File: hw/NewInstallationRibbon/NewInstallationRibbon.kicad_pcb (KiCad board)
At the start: 2 copper layers, 99.7 x 84.5 mm, 34 parts, among them J1 +5V, J10 D4, J11 8 Pin, J12 LEFT, J13 RIGHT, J14 UP, J15 GND, J16 GND, J17 20 Pin, J18 DOWN, J19 R, J2 GND, J20 L, J21 START, J22 B_1, J23 B_2, J25 BRIGHT, J3 CLK, J4 SMS, J5 DW, J6 CL2, J7 D1, J8 D2, J9 D3

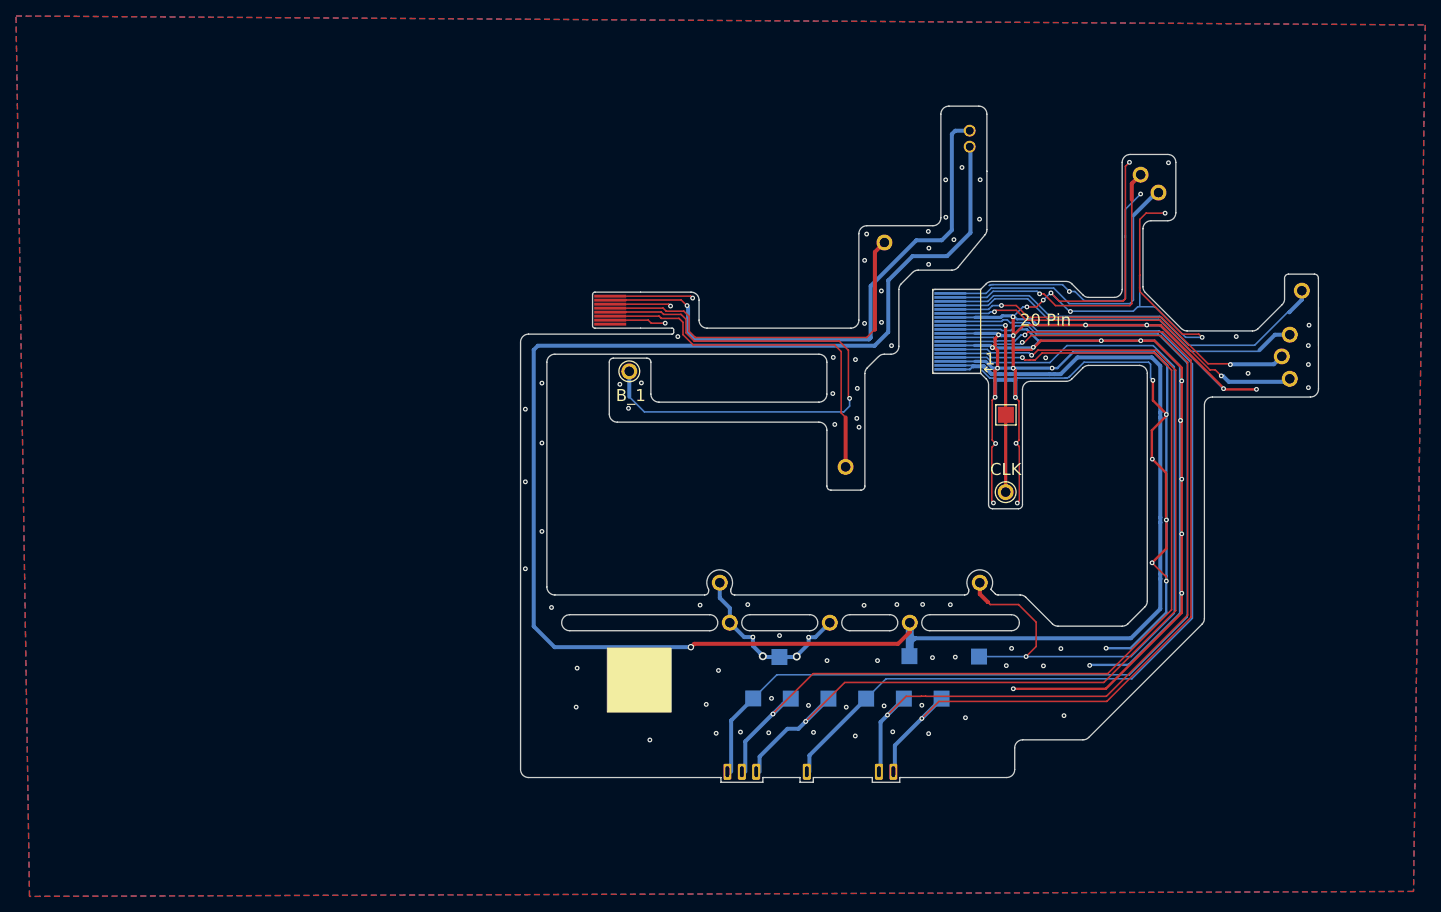
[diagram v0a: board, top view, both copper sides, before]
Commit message: Added LM358 op-amp for both audio channels.
Updated ribbon connector pin assignments, text labels, and tweaked board outline.
Gerbers updated for production.
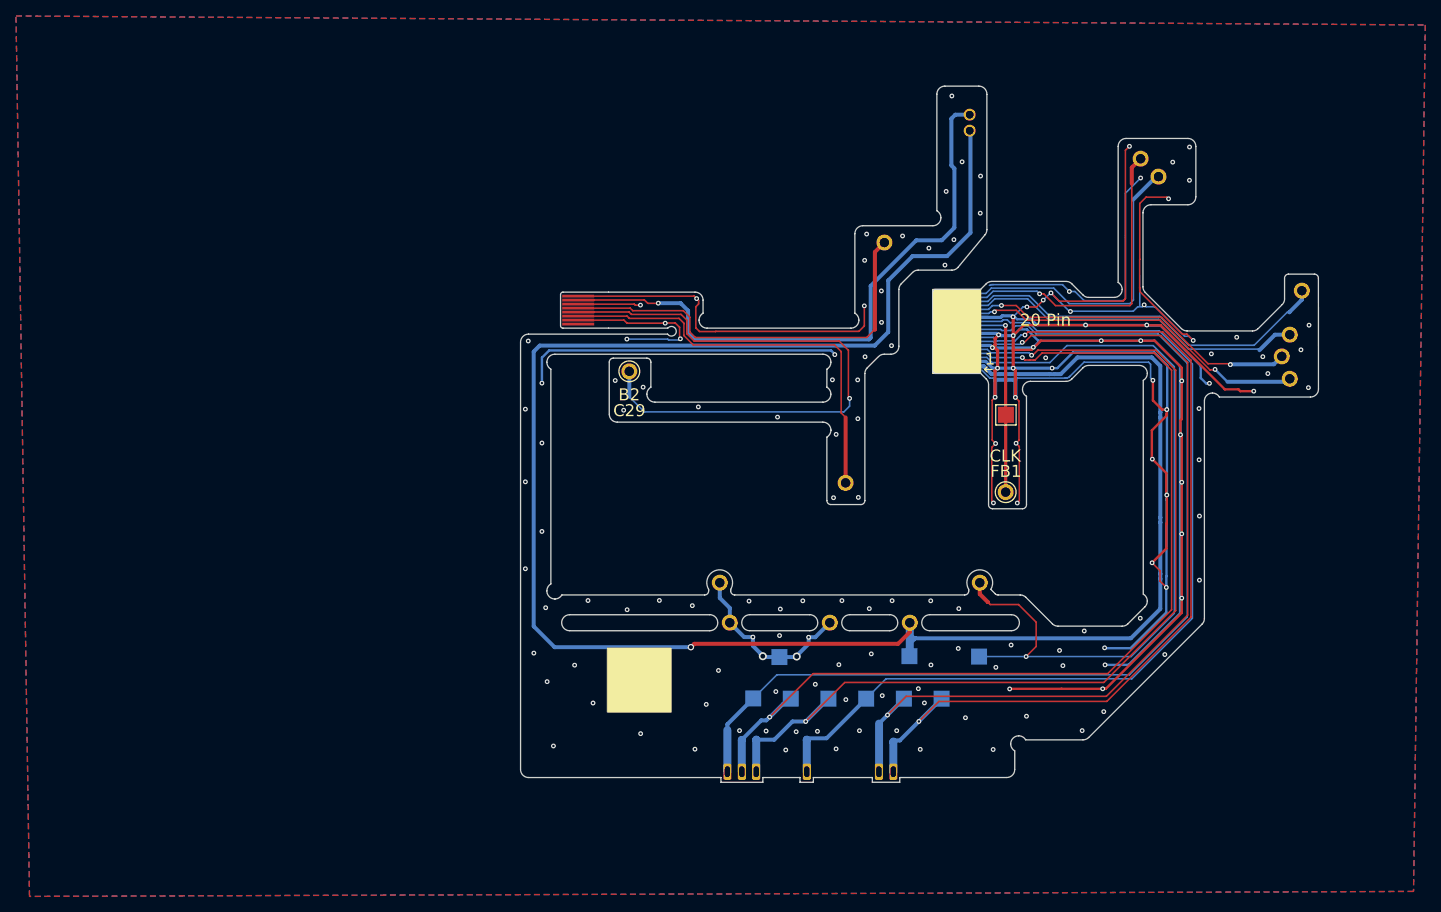
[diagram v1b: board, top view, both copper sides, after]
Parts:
- J1, J12, J13, J14, J15, J16, J18, J19, J2, J20, J21, J3, J4: footprint gg_lcd:TestPoint_THTPad_D2.5mm_Drill1.2mm_OneSided -> gg_lcd:TestPoint_THTPad_D2.5mm_Drill1.2mm
- J22: value B_1 -> B2; footprint gg_lcd:TestPoint_THTPad_D2.5mm_Drill1.2mm_OneSided -> gg_lcd:TestPoint_THTPad_D2.5mm_Drill1.2mm
- J23: value B_2 -> B1; footprint gg_lcd:TestPoint_THTPad_D2.5mm_Drill1.2mm_OneSided -> gg_lcd:TestPoint_THTPad_D2.5mm_Drill1.2mm
- moved J11 4.00 mm to (121.6, 84.5)
- moved J19 2.00 mm to (194.0, 65.6)
- moved J20 2.00 mm to (196.2, 67.8)
- moved J23 2.00 mm to (157.1, 106.1)
- moved J25 2.00 mm to (172.6, 60.1)
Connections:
- J11 pad 5: GG_BTN_1 -> GG_BTN_2
- J11 pad 6: GG_BTN_2 -> GG_BTN_1
- J22 pad 1: GG_BTN_1 -> GG_BTN_2
- J23 pad 1: GG_BTN_2 -> GG_BTN_1
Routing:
- net GND: track 577.2 -> 667.5 mm, vias 125 -> 158
- net GG_BTN_2: track 46.3 -> 77.6 mm, vias 0 -> 1
- net GG_BTN_1: track 73.6 -> 52.3 mm, vias 1 -> 0
- net GG_BRIGHT: track 72.5 -> 78.6 mm
- net GG_BTN_START: track 47.5 -> 51.5 mm
- net GG_AUDIO_R: track 40.4 -> 42.4 mm
- net GG_AUDIO_L: track 39.1 -> 41.1 mm
- net GG_+5V: track 262.6 -> 264.4 mm
- net GG_D2: track 125.6 -> 127.3 mm
- net GG_CL2: track 121.9 -> 123.2 mm
- net GG_D1: track 126.2 -> 127.3 mm
- net GG_D4: track 114.8 -> 115.7 mm
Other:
- board size 99.7 x 84.5 mm -> 99.7 x 87 mm

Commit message: Flex PCB updated:
- Use a single 24pin connection to the main board, pin out updated to match the main board.
- Various layout tweaks to improve installation by reducing some of the slack.
- Added rule areas around solder points to exclude copper fills to help align the solder points.
- Added guide holes for the top row of cartridge connector pins, and tweaked the other guide holes to help with install.
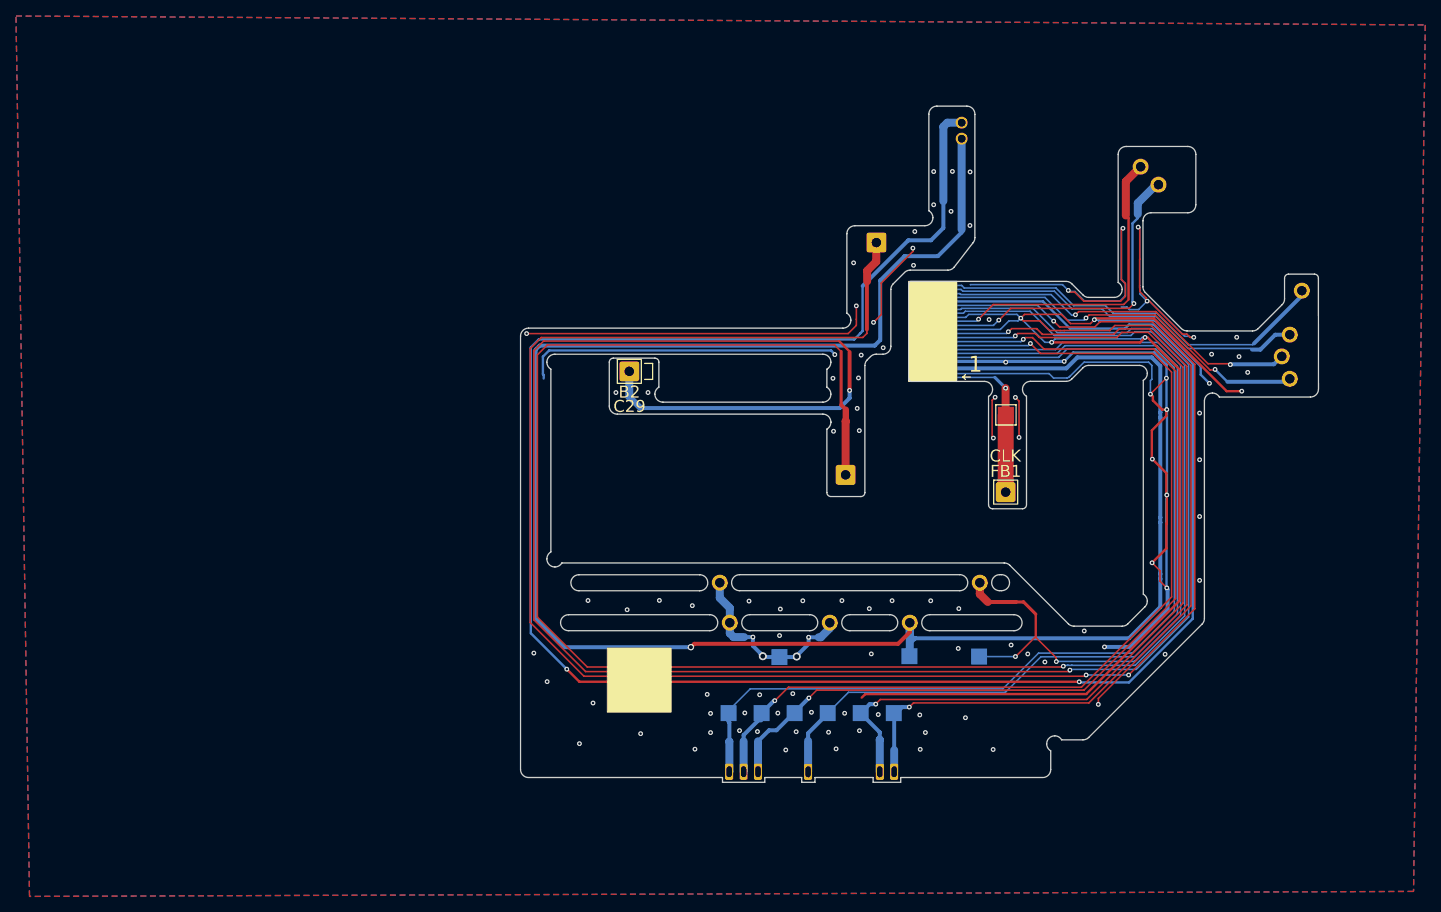
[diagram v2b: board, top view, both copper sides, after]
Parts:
- removed J11: 8 Pin, gg_lcd:Flex Connector 0.5mm 01x08Pin
- J17: value 20 Pin -> 24 Pin Flex Connector; footprint gg_lcd:Flex Connector 0.5mm 01x20Pin -> gg_lcd:Flex Connector 0.5mm 01x24Pin
- J21, J22, J23, J3: footprint gg_lcd:TestPoint_THTPad_D2.5mm_Drill1.2mm -> gg_lcd:TestPoint_THTPad_D2.5x2.5mm_Drill1.2mm
- moved TP7 6.24 mm to (163.2, 134.9)
- moved TP8 5.69 mm to (159.0, 134.9)
- moved TP6 5.14 mm to (154.9, 134.9)
- moved TP9 4.60 mm to (150.8, 134.9)
- moved TP10 4.07 mm to (146.6, 134.9)
- moved TP5 3.58 mm to (142.5, 134.9)
- moved J17 3.00 mm to (165.1, 87.2)
- moved J25 1.41 mm to (171.6, 61.1)
- moved J19 1.00 mm to (194.0, 66.6)
- moved J20 1.00 mm to (196.2, 68.8)
- moved J21 1.00 mm to (161.0, 76.0)
- moved J23 1.00 mm to (157.1, 105.1)
- moved J5 0.23 mm to (142.6, 142.2)
- moved J7 0.22 mm to (144.4, 142.2)
- moved J8 0.22 mm to (146.2, 142.2)
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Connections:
- J17 pad 1: GG_+5V -> GG_CLK
- J17 pad 10: GND -> GG_D2
- J17 pad 11: GG_DW -> GG_D3
- J17 pad 12: GG_CLK -> GG_D4
- J17 pad 13: GG_CL2 -> GND
- J17 pad 14: GND -> GG_AUDIO_L
- J17 pad 15: GG_BTN_DOWN -> GG_AUDIO_R
- J17 pad 16: GG_BTN_LEFT -> GND
- J17 pad 17: GG_BTN_RIGHT -> GG_BTN_1
- J17 pad 18: GG_BTN_UP -> GG_BTN_2
- J17 pad 19: GG_AUDIO_R -> GG_BTN_START
- J17 pad 2: GG_+5V -> GND
- J17 pad 20: GG_AUDIO_L -> GG_BRIGHT
- J17 pad 3: GND -> GG_+5V
- J17 pad 4: GG_SMS -> GG_+5V
- J17 pad 5: GG_D1 -> GND
- J17 pad 6: GG_D2 -> GG_DW
- J17 pad 7: GND -> GG_CL2
- J17 pad 8: GG_D3 -> GG_SMS
- J17 pad 9: GG_D4 -> GG_D1
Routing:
- net GG_BTN_START: track 51.5 -> 246.1 mm, vias 0 -> 3
- net GG_BRIGHT: track 78.6 -> 270.3 mm, vias 1 -> 2
- net GG_BTN_2: track 77.6 -> 267.3 mm, vias 1 -> 2
- net GG_BTN_1: track 52.3 -> 240.4 mm, vias 0 -> 1
- net GND: track 667.5 -> 605.9 mm, vias 158 -> 110
- net GG_SMS: track 102.5 -> 107.1 mm, vias 1 -> 2
- net GG_CLK: track 27.8 -> 23.5 mm
- net GG_BTN_DOWN: track 46.5 -> 50.6 mm
- net GG_BTN_LEFT: track 45.1 -> 48.9 mm
- net GG_BTN_RIGHT: track 46.2 -> 49.3 mm
- net GG_BTN_UP: track 50.3 -> 53.2 mm
- net GG_D2: track 127.3 -> 124.8 mm
- net GG_AUDIO_L: track 41.1 -> 43.5 mm, vias 0 -> 2
- net GG_CL2: track 123.2 -> 121.0 mm
- net GG_D1: track 127.3 -> 125.2 mm
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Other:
- board size 99.7 x 87 mm -> 99.7 x 84.5 mm
